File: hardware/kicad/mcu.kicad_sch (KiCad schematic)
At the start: 8 parts, among them J2 SWD/UART Recovery (DNP), J5 1x15 P2.54 mm female socket (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, J6 1x15 P2.54 mm female socket (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

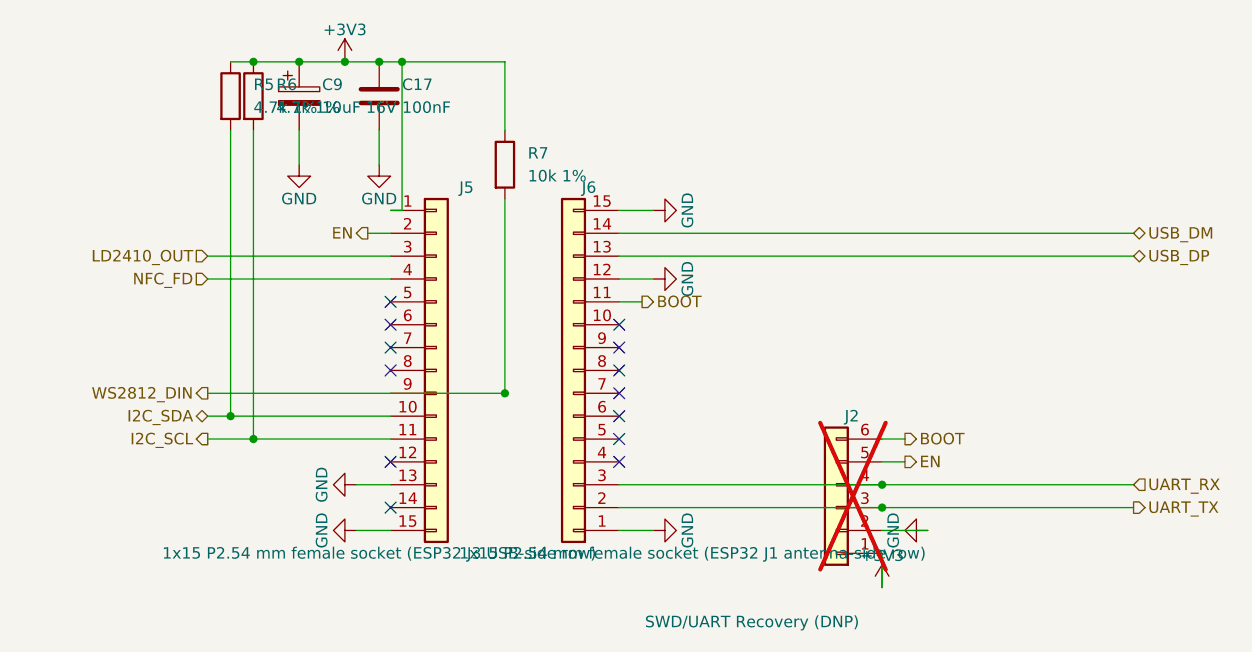
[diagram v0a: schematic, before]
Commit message: fix(schematic): C9 non-polarized symbol + J2 label + doc drifts
Closes the remaining items from the 50-agent connectivity audit.

C9 (10 uF MLCC, Samsung CL21A106KAYNNNE — verified ceramic / X5R,
non-polarized) was drawn with Device:C_Polarized, implying a polarity
constraint the part does not have. Switch to Device:C. Connectivity is
unchanged: pin geometry is identical and the +3V3 / GND nets keep
their names.

J2 recovery header was labelled "SWD/UART Recovery" — the ESP32-C6 is
RISC-V and exposes no SWD; the header carries UART + EN + BOOT. Renamed
to "UART/Boot Recovery (DNP)" across BOTH the schematic generator and
the PCB footprint generator (the value string lives in each).

Doc drifts: CLAUDE.md F1 row corrected 2920L075/60MR (C207083) ->
1812L075THDR (C262023) to match the BOM / lcsc_mapping; _sch_mcu.py
GPIO16/17 comments corrected UART0 -> UART1.

29/29 build PASS — DRC 0, ERC 0, determinism OK.

Co-Authored-By: Claude Opus 4.7 <noreply@anthropic.com>
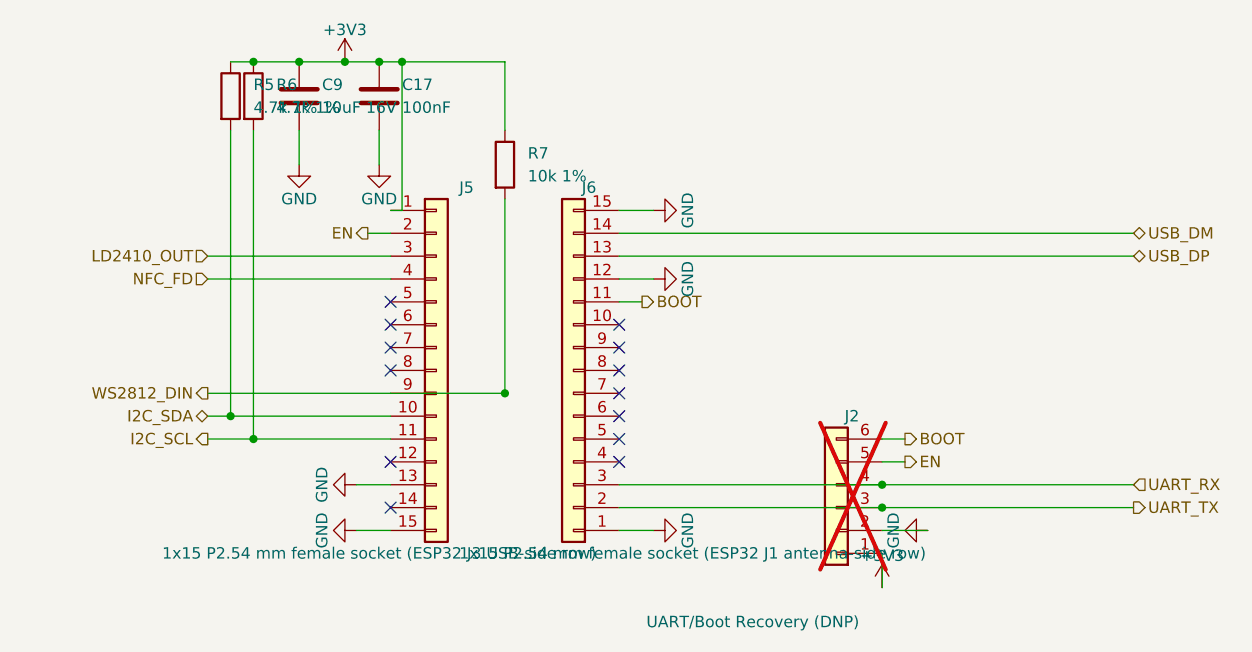
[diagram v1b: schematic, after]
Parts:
- C9: symbol Device:C_Polarized -> Device:C
- J2: value SWD/UART Recovery (DNP) -> UART/Boot Recovery (DNP)
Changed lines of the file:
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@@
         			)
         		)
-        		(property "Value" "SWD/UART Recovery (DNP)"
+        		(property "Value" "UART/Boot Recovery (DNP)"
         			(at 191.77 138.43 0)
         			(effects
@@
         	)
 (symbol
-	(lib_id "Device:C_Polarized")
+	(lib_id "Device:C")
 	(at 129.54 80.01 0)
 	(unit 1)

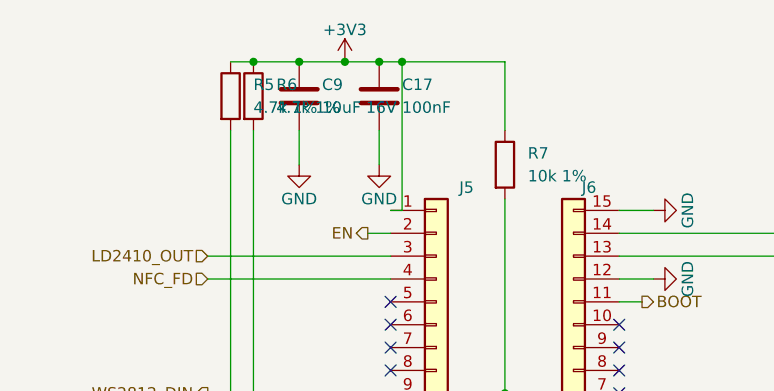
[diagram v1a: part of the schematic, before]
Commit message: fix(bom): align C5/C9 + F1 voltage labels to the actual sourced parts
C5/C9 (Samsung CL21A106KAYNNNE) — verified against the Samsung
datasheet as 10 uF / 25 V / X5R / 0805. The schematic Value and the
lcsc_mapping key said "10uF 16V" (the v0.5 reviewer's design minimum),
understating the real part. Relabelled "10uF 16V" -> "10uF 25V".

F1 (Littelfuse 1812L075THDR) — lcsc_mapping carried an internal
contradiction: the key said "PTC 750mA / 60V" (stale — carried over
from the superseded 2920L075/60MR) while the entry's own notes already
said 75 V max. The 2920->1812 swap was made so the footprint can reuse
KiCad's stock R_1812_4532Metric STEP model. Relabelled "/ 60V" ->
"/ 75V" to match the notes; CLAUDE.md F1 row updated to 75 V. The
lcsc_mapping "VERIFY LCSC# at order time" note is kept.

LCSC#s (C15850, C262023) unchanged. BOM regenerated. 29/29 PASS.

Co-Authored-By: Claude Opus 4.7 <noreply@anthropic.com>
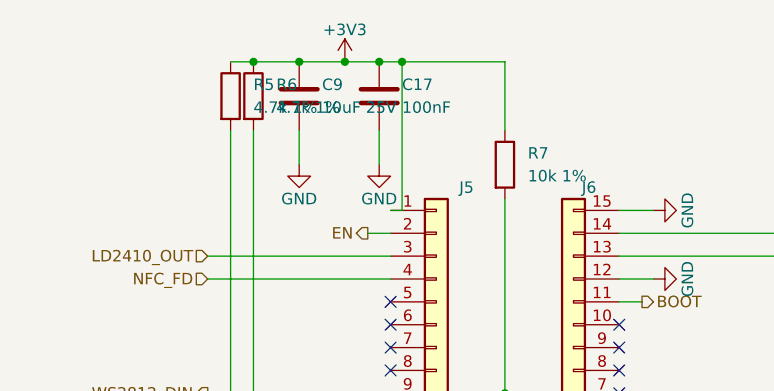
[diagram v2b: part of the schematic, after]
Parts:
- C9: value 10uF 16V -> 10uF 25V
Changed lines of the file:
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@@
 		)
 	)
-	(property "Value" "10uF 16V"
+	(property "Value" "10uF 25V"
 		(at 132.08 81.28 0)
 		(effects

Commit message: hardware+firmware: remove the dynamic NFC tag (MIKROE-2462 / NT3H1101)
Closes #7.

The NFC feature is dropped entirely: RF coupling through the AK-N-94
cover is unusable as integrated, the only workable fix (cover-mounted
antenna) breaks the aesthetic pillar, and the LED ring + HA dashboard
already cover the need. Recorded in CLAUDE.md Out-of-scope.

Hardware (boardgen):
- MOD2 (oas:MIKROE-2462_Reference), J7 + J8 mikroBUS sockets and C12
  decoupling removed from schematic, placement, footprints, Z-clearance
  and the stage-18 whitelist (9 -> 8 documented customs).
- GPIO 3 (net NFC_FD) freed -> spare no_connect, same pattern as GPIO 1
  in the SW1 removal; ten spare safe-non-strap GPIOs now.
- Routing snapshot 600 seg + 40 via -> 586 seg + 43 via: /MCU/NFC_FD
  (2 seg) and 12 dead GND stitches anchored at the removed pads swept;
  3 bridge vias added where former J7.7/J8.5/J8.6 THT pads carried the
  live +3V3 / I2C_SCL / I2C_SDA layer transitions feeding the SEN66
  (J3). Clearance at the via spots >= 0.71 mm vs the 0.20 mm rule.
- I2C bus is now SEN66 + Qwiic; stage 26 rise time improves to
  278/277 ns (was 306/305) vs the 1000 ns Standard-mode ceiling.
- POWER_BUDGET, EXTERNAL_MODULES, THT_REFERENCES, tests and BOM/CPL
  deliverables updated; dead 2x8-connector schematic helper removed.

Firmware (esphome):
- packages/nfc.yaml deleted; dashboard_url substitution and all NFC
  references removed from oas.yaml, package comments and READMEs.
- HARDWARE-COMPAT-v0.51.md: removal recorded as final; the five v0.51
  boards keep unpopulated J7/J8/MOD2 footprints.

Verification: implemented and adversarially reviewed by two independent
agents; build.py 35/35 PASS on both runs; DRC 0 violations /
0 unconnected; ERC 0/0; F.Cu pour refills the former mikroBUS field
with no orphan islands; deliverables (BOM/CPL/gerbers/ibom) carry zero
NFC references.

Co-Authored-By: Claude Fable 5 <noreply@anthropic.com>
Claude-Session: https://claude.ai/code/session_017QqgHNrNySNTKB44F1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
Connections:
- net NFC_FD: no longer names the net of J5.4 (Pin_4)
- no-connect marks 13 -> 14
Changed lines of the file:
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@@
-(wire
-	(pts
-		(xy 139.7 100.33) (xy 119.38 100.33)
-	)
-	(stroke
-		(width 0)
-		(type default)
-	)
-)
 (wire
 	(pts
@@
 	)
 )
-(hierarchical_label "NFC_FD"
-	(shape input)
-	(at 119.38 100.33 180)
-	(effects
-		(font
-			(size 1.27 1.27)
-		)
-		(justify right)
-	)
-)
 (hierarchical_label "WS2812_DIN"
 	(shape output)
@@
 )
 (no_connect
+	(at 139.7 100.33)
+)
+(no_connect

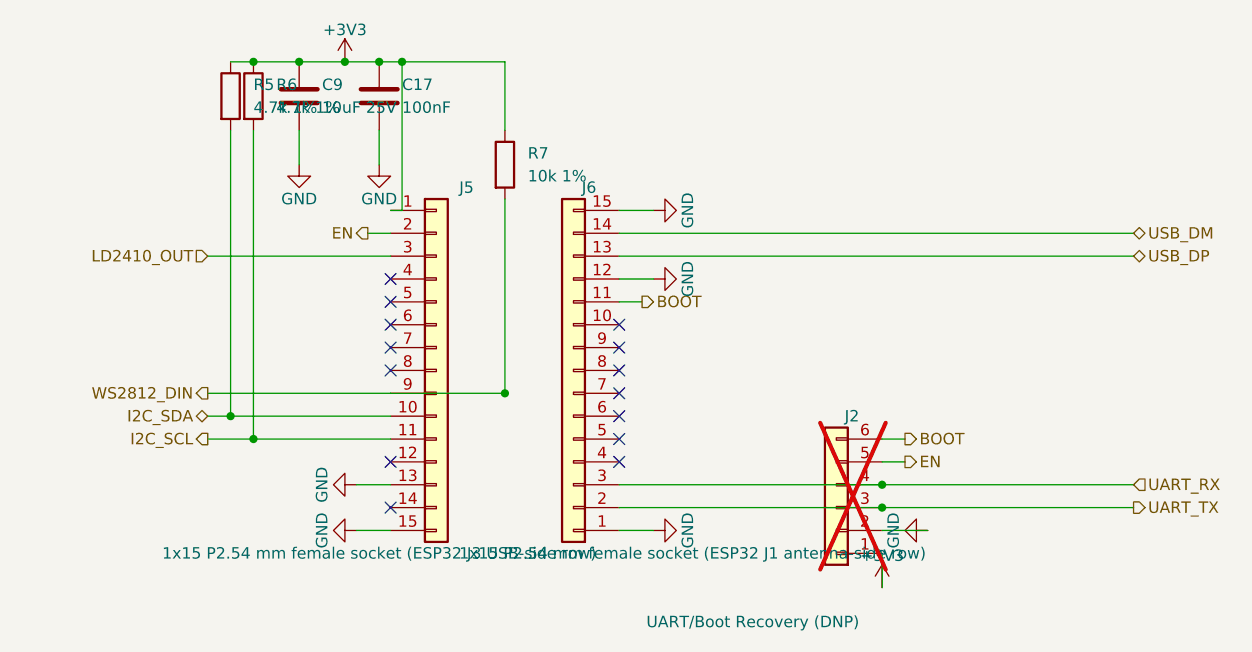
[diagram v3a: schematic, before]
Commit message: hardware+firmware: move the LD2410 UART off GPIO16/17 (CP2102N contention)
The LD2410 UART sat on GPIO16/17 from v0.4 on the reasoning that those are
"just the default UART0 pins" and the C6's GPIO matrix can re-route UART0.
That reasoning covers the SoC only. On the ESP32-C6-DevKitM-1 the same two
pads are wired through populated 0 R links (R9 -> CP2102N RXD pin 25,
R7 -> CP2102N TXD pin 26) to the onboard USB-UART bridge, and that bridge's
VDD (6) + REGIN (7) tie to VCC_3V3 -- the board rail OAS drives at J5.1 --
not to USB VBUS (pin 8 only sees the R19/R18 sense divider). So the bridge
is powered whenever the unit is, and its TXD is a push-pull output parked
on the ESP's RX net. Two drivers, one node.

Bench-proved on a v0.51 board with the radar unpowered (24 V off) and the
bridge's own USB port empty, probing with the ESP's internal pulls:
  GPIO2  pu=1/pd=0  FLOATING
  GPIO16 pu=1/pd=0  FLOATING
  GPIO17 pu=1/pd=1  DRIVEN
The two control pins follow the pulls; GPIO17 holds HIGH against its own
pull-down with nothing on that net but the bridge's TXD.

Fix: the pair moves to GPIO 1 (TX) / GPIO 0 (RX) -- free, adjacent,
non-strap pads on J5, the socket row nearest J4. Nets renamed
LD2410_UART_TX / LD2410_UART_RX; UART_TX / UART_RX stay as the true console
on GPIO16/17, reaching only the DNP recovery header J2 (that header exists
to serial-flash a module whose USB ports are dead, so it belongs on the ROM
bootloader's own pins and must not follow a peripheral around).

GPIO16/17 move into GPIO_RESERVED, and stage 06 grows a console-pin check
that fails if any refdes other than J6/J2 appears on either console net --
a dict entry is a comment, a check is a guarantee.

Replacement pins vetted the same way the old ones failed: GPIO0/1 double as
XTAL_32K_P/N and the DevKitM-1 does carry that network, but Y1, C4/C5 and
R1 are all (NC) on the Espressif schematic and only the 0 R links R3/R2 to
the header are populated -- the pads are electrically bare.

Firmware gains ld2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
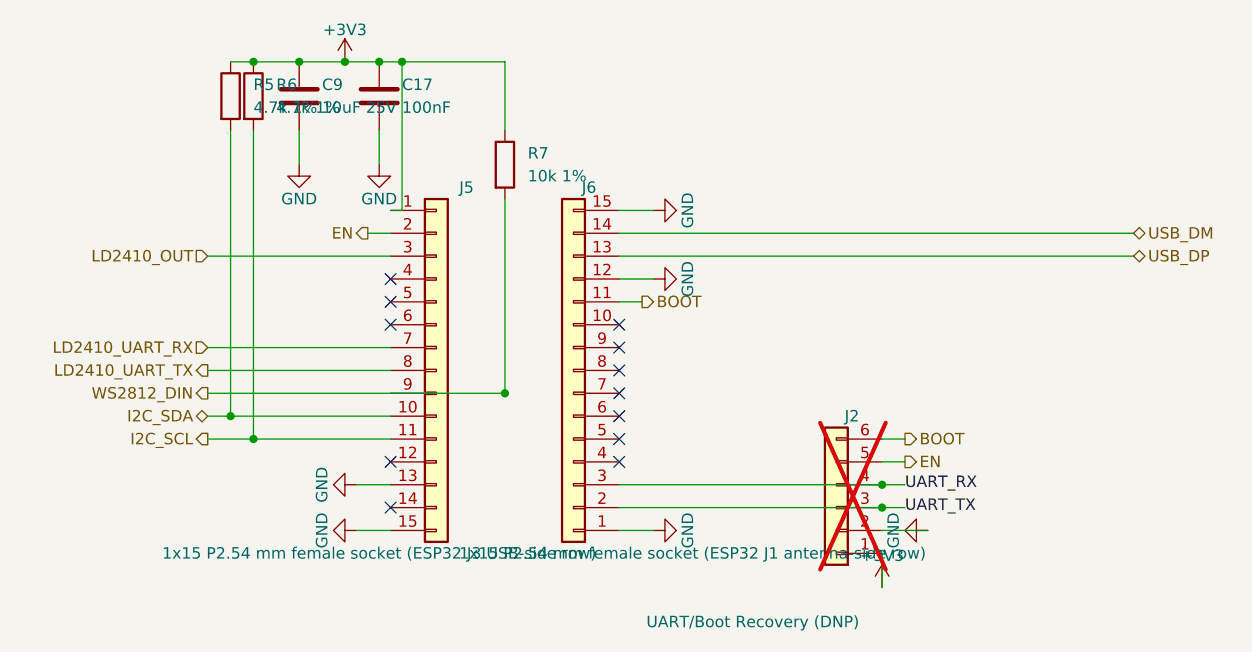
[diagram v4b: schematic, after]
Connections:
- net LD2410_UART_RX: now reaches J5.7 (Pin_7)
- net LD2410_UART_TX: now reaches J5.8 (Pin_8)
- no-connect marks 14 -> 12
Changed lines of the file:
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@@
+(wire
+	(pts
+		(xy 139.7 107.95) (xy 119.38 107.95)
+	)
+	(stroke
+		(width 0)
+		(type default)
+	)
+)
+(wire
+	(pts
+		(xy 139.7 110.49) (xy 119.38 110.49)
+	)
+	(stroke
+		(width 0)
+		(type default)
+	)
+)
 (wire
 	(pts
@@
 (wire
 	(pts
-		(xy 165.1 125.73) (xy 222.25 125.73)
+		(xy 165.1 125.73) (xy 196.85 125.73)
 	)
 	(stroke
@@
 	(color 0 0 0 0)
 )
-(wire
-	(pts
-		(xy 165.1 123.19) (xy 222.25 123.19)
+(label "UART_TX"
+	(at 196.85 125.73 0)
+	(effects
+		(font
+			(size 1.27 1.27)
+		)
+		(justify left)
+	)
+)
+(wire
+	(pts
+		(xy 165.1 123.19) (xy 196.85 123.19)
 	)
 	(stroke
@@
 	(diameter 0)
 	(color 0 0 0 0)
+)
+(label "UART_RX"
+	(at 196.85 123.19 0)
+	(effects
+		(font
+			(size 1.27 1.27)
+		)
+		(justify left)
+	)
 )
 (wire
@@
 	)
 )
-(hierarchical_label "UART_TX"
+(hierarchical_label "LD2410_UART_RX"
+	(shape input)
+	(at 119.38 107.95 180)
+	(effects
+		(font
+			(size 1.27 1.27)
+		)
+		(justify right)
+	)
+)
+(hierarchical_label "LD2410_UART_TX"
 	(shape output)
-	(at 222.25 125.73 0)
-	(effects
-		(font
-			(size 1.27 1.27)
-		)
-		(justify left)
-	)
-)
-(hierarchical_label "UART_RX"
-	(shape input)
-	(at 222.25 123.19 0)
-	(effects
-		(font
-			(size 1.27 1.27)
-		)
-		(justify left)
+	(at 119.38 110.49 180)
+	(effects
+		(font
+			(size 1.27 1.27)
+		)
+		(justify right)
 	)
 )
@@
 )
 (no_connect
-	(at 139.7 107.95)
-)
-(no_connect
-	(at 139.7 110.49)
-)
-(no_connect
